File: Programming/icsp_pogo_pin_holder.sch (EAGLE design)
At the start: 4 parts

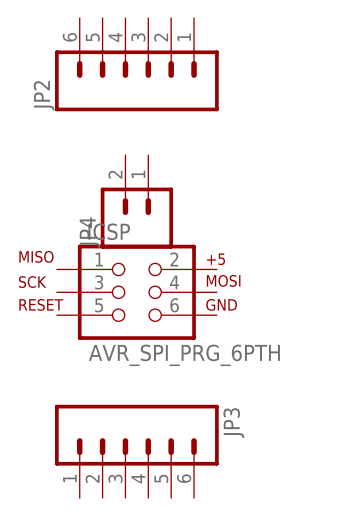
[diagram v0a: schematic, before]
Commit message: increased pogo pin hole size in icsp header
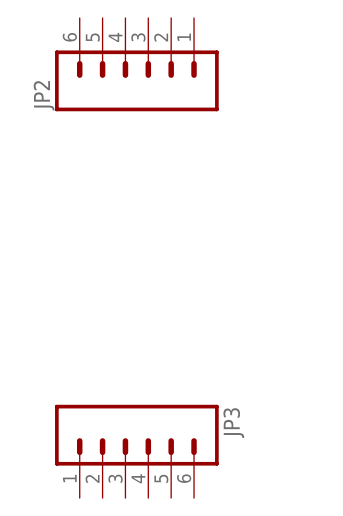
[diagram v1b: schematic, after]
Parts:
- removed ICSP: AVR_SPI_PRG_6PTH, SparkFun-Connectors:AVR_SPI_PRG_6PTH
- removed JP4: (no value), SparkFun-Connectors:M02PTH
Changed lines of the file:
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@@
 <grid distance="0.1" unitdist="inch" unit="inch" style="lines" multiple="1" display="no" altdistance="0.01" altunitdist="inch" altunit="inch"/>
 <layers>
-<layer number="1" name="Top" color="4" fill="1" visible="no" active="no"/>
-<layer number="16" name="Bottom" color="1" fill="1" visible="no" active="no"/>
-<layer number="17" name="Pads" color="2" fill="1" visible="no" active="no"/>
-<layer number="18" name="Vias" color="2" fill="1" visible="no" active="no"/>
-<layer number="19" name="Unrouted" color="6" fill="1" visible="no" active="no"/>
-<layer number="20" name="Dimension" color="15" fill="1" visible="no" active="no"/>
-<layer number="21" name="tPlace" color="16" fill="1" visible="no" active="no"/>
-<layer number="22" name="bPlace" color="7" fill="1" visible="no" active="no"/>
-<layer number="23" name="tOrigins" color="15" fill="1" visible="no" active="no"/>
-<layer number="24" name="bOrigins" color="15" fill="1" visible="no" active="no"/>
-<layer number="25" name="tNames" color="7" fill="1" visible="no" active="no"/>
-<layer number="26" name="bNames" color="7" fill="1" visible="no" active="no"/>
-<layer number="27" name="tValues" color="7" fill="1" visible="no" active="no"/>
-<layer number="28" name="bValues" color="7" fill="1" visible="no" active="no"/>
+<layer number="1" name="Top" color="4" fill="1" visible="yes" active="no"/>
+<layer number="16" name="Bottom" color="1" fill="1" visible="yes" active="no"/>
+<layer number="17" name="Pads" color="2" fill="1" visible="yes" active="no"/>
+<layer number="18" name="Vias" color="2" fill="1" visible="yes" active="no"/>
+<layer number="19" name="Unrouted" color="6" fill="1" visible="yes" active="no"/>
+<layer number="20" name="Dimension" color="15" fill="1" visible="yes" active="no"/>
+<layer number="21" name="tPlace" color="7" fill="1" visible="yes" active="no"/>
+<layer number="22" name="bPlace" color="7" fill="1" visible="yes" active="no"/>
+<layer number="23" name="tOrigins" color="15" fill="1" visible="yes" active="no"/>
+<layer number="24" name="bOrigins" color="15" fill="1" visible="yes" active="no"/>
+<layer number="25" name="tNames" color="7" fill="1" visible="yes" active="no"/>
+<layer number="26" name="bNames" color="7" fill="1" visible="yes" active="no"/>
+<layer number="27" name="tValues" color="7" fill="1" visible="yes" active="no"/>
+<layer number="28" name="bValues" color="7" fill="1" visible="yes" active="no"/>
 <layer number="29" name="tStop" color="7" fill="3" visible="no" active="no"/>
 <layer number="30" name="bStop" color="7" fill="6" visible="no" active="no"/>
@@
 <layer number="35" name="tGlue" color="7" fill="4" visible="no" active="no"/>
 <layer number="36" name="bGlue" color="7" fill="5" visible="no" active="no"/>
-<layer number="37" name="tTest" color="7" fill="1" visible="no" active="no"/>
-<layer number="38" name="bTest" color="7" fill="1" visible="no" active="no"/>
+<layer number="37" name="tTest" color="7" fill="1" visible="yes" active="no"/>
+<layer number="38" name="bTest" color="7" fill="1" visible="yes" active="no"/>
 <layer number="39" name="tKeepout" color="4" fill="11" visible="no" active="no"/>
 <layer number="40" name="bKeepout" color="1" fill="11" visible="no" active="no"/>
@@
 <layer number="44" name="Drills" color="7" fill="1" visible="no" active="no"/>
 <layer number="45" name="Holes" color="7" fill="1" visible="no" active="no"/>
-<layer number="46" name="Milling" color="3" fill="1" visible="no" active="no"/>
-<layer number="47" name="Measures" color="7" fill="1" visible="no" active="no"/>
-<layer number="48" name="Document" color="7" fill="1" visible="no" active="no"/>
-<layer number="49" name="Reference" color="7" fill="1" visible="no" active="no"/>
-<layer number="50" name="dxf" color="7" fill="1" visible="no" active="no"/>
-<layer number="51" name="tDocu" color="14" fill="1" visible="no" active="no"/>
-<layer number="52" name="bDocu" color="7" fill="1" visible="no" active="no"/>
-<layer number="53" name="tGND_GNDA" color="7" fill="9" visible="no" active="no"/>
-<layer number="54" name="bGND_GNDA" color="1" fill="9" visible="no" active="no"/>
-<layer number="56" name="wert" color="7" fill="1" visible="no" active="no"/>
-<layer number="57" name="tCAD" color="7" fill="1" visible="no" active="no"/>
-<layer number="59" name="tCarbon" color="7" fill="1" visible="no" active="no"/>
-<layer number="60" name="bCarbon" color="7" fill="1" visible="no" active="no"/>
+<layer number="46" name="Milling" color="3" fill="1" visible="yes" active="no"/>
+<layer number="47" name="Measures" color="7" fill="1" visible="yes" active="no"/>
+<layer number="48" name="Document" color="7" fill="1" visible="yes" active="no"/>
+<layer number="49" name="Reference" color="7" fill="1" visible="yes" active="no"/>
+<layer number="50" name="dxf" color="7" fill="1" visible="yes" active="no"/>
+<layer number="51" name="tDocu" color="7" fill="1" visible="yes" active="no"/>
+<layer number="52" name="bDocu" color="7" fill="1" visible="yes" active="no"/>
+<layer number="53" name="tGND_GNDA" color="7" fill="9" visible="yes" active="no"/>
+<layer number="54" name="bGND_GNDA" color="1" fill="9" visible="yes" active="no"/>
+<layer number="56" name="wert" color="7" fill="1" visible="yes" active="no"/>
+<layer number="57" name="tCAD" color="7" fill="1" visible="yes" active="no"/>
+<layer number="59" name="tCarbon" color="7" fill="1" visible="yes" active="no"/>
+<layer number="60" name="bCarbon" color="7" fill="1" visible="yes" active="no"/>
 <layer number="90" name="Modules" color="5" fill="1" visible="yes" active="yes"/>
 <layer number="91" name="Nets" color="2" fill="1" visible="yes" active="yes"/>
@@
 </classes>
 <parts>
-<part name="ICSP" library="SparkFun-Connectors" deviceset="AVR_SPI_PRG_6" device="PTH"/>
 <part name="JP2" library="SparkFun-Connectors" deviceset="M06" device="NO_SILK_FEMALE_PTH"/>
 <part name="JP3" library="SparkFun-Connectors" deviceset="M06" device="NO_SILK_FEMALE_PTH"/>
-<part name="JP4" library="SparkFun-Connectors" deviceset="M02" device="PTH"/>
 </parts>
 <sheets>
@@
 </plain>
 <instances>
-<instance part="ICSP" gate="G$1" x="38.1" y="58.42"/>
 <instance part="JP2" gate="G$1" x="40.64" y="83.82" rot="R90"/>
 <instance part="JP3" gate="G$1" x="38.1" y="40.64" rot="R270"/>
-<instance part="JP4" gate="G$1" x="40.64" y="66.04" rot="R90"/>
 </instances>
 <busses>
